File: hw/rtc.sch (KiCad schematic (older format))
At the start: 5 parts, among them U5 PCF8563T, Y1 Crystal_Small

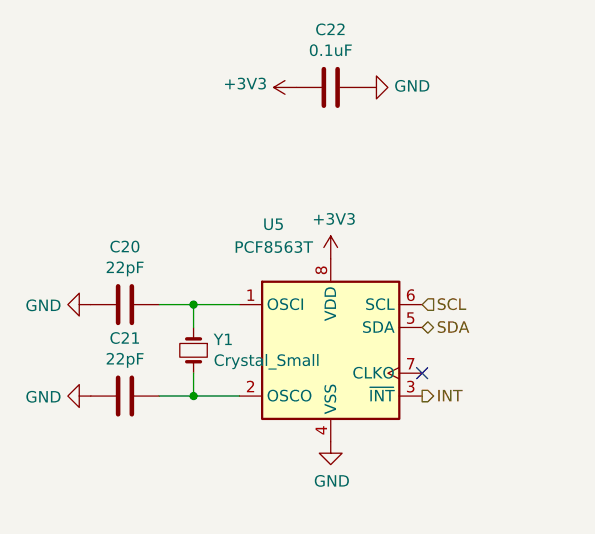
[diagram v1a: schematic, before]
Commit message: epd-clock: hw add wakeup pin pull up register
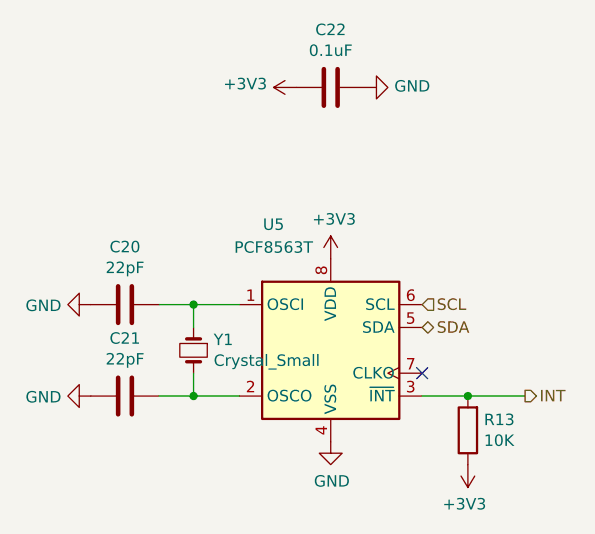
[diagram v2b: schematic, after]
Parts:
- added R13: 10K, Resistor_SMD:R_0603_1608Metric, symbol Device:R
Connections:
- net +3V3: now also R13.1
- net INT: now also R13.2
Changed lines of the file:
@@
 Text HLabel 6100 3800 2    50   BiDi ~ 0
 SDA
-Text HLabel 6100 4100 2    50   Output ~ 0
+Text HLabel 6550 4100 2    50   Output ~ 0
 INT
 NoConn ~ 6100 4000
+$Comp
+L Device:R R13
+U 1 1 6118B5C6
+P 6300 4250
+F 0 "R13" H 6230 4204 50  0000 R CNN
+F 1 "10K" H 6230 4295 50  0000 R CNN
+F 2 "Resistor_SMD:R_0603_1608Metric" V 6230 4250 50  0001 C CNN
+F 3 "~" H 6300 4250 50  0001 C CNN
+	1    6300 4250
+	-1   0    0    1
+$EndComp
+Wire Wire Line
+	6100 4100 6300 4100
+Connection ~ 6300 4100
+Wire Wire Line
+	6300 4100 6550 4100
+$Comp
+L power:+3V3 #PWR056
+U 1 1 6118BF3A
+P 6300 4400
+F 0 "#PWR056" H 6300 4250 50  0001 C CNN
+F 1 "+3V3" H 6315 4573 50  0000 C CNN
+F 2 "" H 6300 4400 50  0001 C CNN
+F 3 "" H 6300 4400 50  0001 C CNN
+	1    6300 4400
+	-1   0    0    1
+$EndComp
 $EndSCHEMATC

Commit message: epd-clock: hw: v0.2
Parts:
- renumbered C20 to C19, C21 to C20, C22 to C21, R13 to R18, U5 to U4
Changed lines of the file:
@@
 $EndDescr
 $Comp
-L Timer_RTC:PCF8563T U5
+L Timer_RTC:PCF8563T U4
 U 1 1 6123A351
 P 5700 3900
-F 0 "U5" H 5450 4450 50  0000 C CNN
+F 0 "U4" H 5450 4450 50  0000 C CNN
 F 1 "PCF8563T" H 5450 4350 50  0000 C CNN
 F 2 "Package_SO:SOIC-8_3.9x4.9mm_P1.27mm" H 5700 3900 50  0001 C CNN
@@
 $EndComp
 $Comp
-L Device:C C22
+L Device:C C21
 U 1 1 61243BFA
 P 5700 2750
-F 0 "C22" V 5448 2750 50  0000 C CNN
+F 0 "C21" V 5448 2750 50  0000 C CNN
 F 1 "0.1uF" V 5539 2750 50  0000 C CNN
 F 2 "Capacitor_SMD:C_0603_1608Metric" H 5738 2600 50  0001 C CNN
@@
 $EndComp
 $Comp
-L power:GND #PWR055
+L power:GND #PWR053
 U 1 1 61244BCB
 P 5850 2750
-F 0 "#PWR055" H 5850 2500 50  0001 C CNN
+F 0 "#PWR053" H 5850 2500 50  0001 C CNN
 F 1 "GND" V 5855 2622 50  0000 R CNN
 F 2 "" H 5850 2750 50  0001 C CNN
@@
 $EndComp
 $Comp
-L power:+3V3 #PWR052
+L power:+3V3 #PWR050
 U 1 1 6124514E
 P 5550 2750
-F 0 "#PWR052" H 5550 2600 50  0001 C CNN
+F 0 "#PWR050" H 5550 2600 50  0001 C CNN
 F 1 "+3V3" V 5565 2878 50  0000 L CNN
 F 2 "" H 5550 2750 50  0001 C CNN
@@
 $EndComp
 $Comp
-L power:+3V3 #PWR053
+L power:+3V3 #PWR051
 U 1 1 6124583B
 P 5700 3500
-F 0 "#PWR053" H 5700 3350 50  0001 C CNN
+F 0 "#PWR051" H 5700 3350 50  0001 C CNN
 F 1 "+3V3" H 5715 3673 50  0000 C CNN
 F 2 "" H 5700 3500 50  0001 C CNN
@@
 $EndComp
 $Comp
-L power:GND #PWR054
+L power:GND #PWR052
 U 1 1 61245C79
 P 5700 4300
-F 0 "#PWR054" H 5700 4050 50  0001 C CNN
+F 0 "#PWR052" H 5700 4050 50  0001 C CNN
 F 1 "GND" H 5705 4127 50  0000 C CNN
 F 2 "" H 5700 4300 50  0001 C CNN
@@
 $EndComp
 $Comp
-L Device:C C20
+L Device:C C19
 U 1 1 612485A7
 P 4800 3700
-F 0 "C20" V 4548 3700 50  0000 C CNN
+F 0 "C19" V 4548 3700 50  0000 C CNN
 F 1 "22pF" V 4639 3700 50  0000 C CNN
 F 2 "Capacitor_SMD:C_0603_1608Metric" H 4838 3550 50  0001 C CNN
@@
 $EndComp
 $Comp
-L Device:C C21
+L Device:C C20
 U 1 1 61248D49
 P 4800 4100
-F 0 "C21" V 4548 4100 50  0000 C CNN
+F 0 "C20" V 4548 4100 50  0000 C CNN
 F 1 "22pF" V 4639 4100 50  0000 C CNN
 F 2 "Capacitor_SMD:C_0603_1608Metric" H 4838 3950 50  0001 C CNN
@@
 	5100 3700 5300 3700
 $Comp
-L power:GND #PWR050
+L power:GND #PWR048
 U 1 1 61249AC1
 P 4650 3700
-F 0 "#PWR050" H 4650 3450 50  0001 C CNN
+F 0 "#PWR048" H 4650 3450 50  0001 C CNN
 F 1 "GND" V 4655 3572 50  0000 R CNN
 F 2 "" H 4650 3700 50  0001 C CNN
@@
 $EndComp
 $Comp
-L power:GND #PWR051
+L power:GND #PWR049
 U 1 1 61249FBE
 P 4650 4100
-F 0 "#PWR051" H 4650 3850 50  0001 C CNN
+F 0 "#PWR049" H 4650 3850 50  0001 C CNN
 F 1 "GND" V 4655 3972 50  0000 R CNN
 F 2 "" H 4650 4100 50  0001 C CNN
@@
 NoConn ~ 6100 4000
 $Comp
-L Device:R R13
+L Device:R R18
 U 1 1 6118B5C6
 P 6300 4250
-F 0 "R13" H 6230 4204 50  0000 R CNN
+F 0 "R18" H 6230 4204 50  0000 R CNN
 F 1 "10K" H 6230 4295 50  0000 R CNN
 F 2 "Resistor_SMD:R_0603_1608Metric" V 6230 4250 50  0001 C CNN
@@
 	6300 4100 6550 4100
 $Comp
-L power:+3V3 #PWR056
+L power:+3V3 #PWR054
 U 1 1 6118BF3A
 P 6300 4400
-F 0 "#PWR056" H 6300 4250 50  0001 C CNN
+F 0 "#PWR054" H 6300 4250 50  0001 C CNN
 F 1 "+3V3" H 6315 4573 50  0000 C CNN
 F 2 "" H 6300 4400 50  0001 C CNN

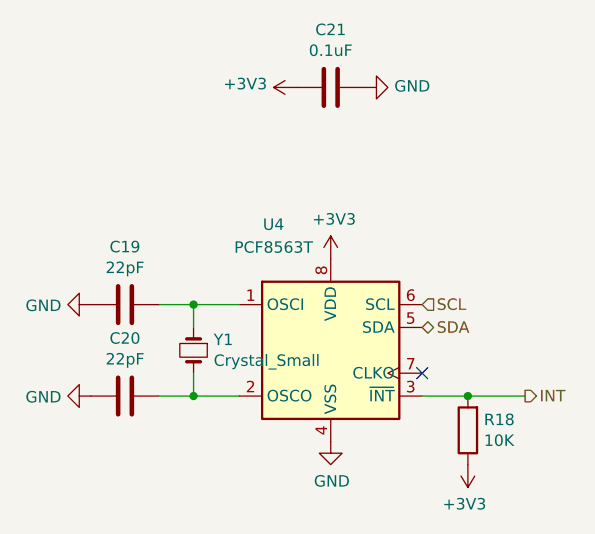
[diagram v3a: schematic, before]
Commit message: hw: 合并电源网络
取消墨水屏电源控制mos与独立电源域，墨水屏使用深度休眠模式，共用主
电源域。
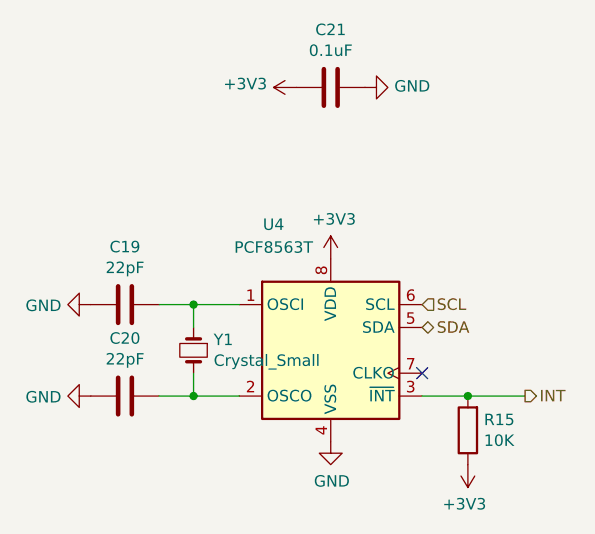
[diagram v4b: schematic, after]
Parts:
- renumbered R18 to R15
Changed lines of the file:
@@
 $EndComp
 $Comp
-L power:GND #PWR053
+L power:GND #PWR051
 U 1 1 61244BCB
 P 5850 2750
-F 0 "#PWR053" H 5850 2500 50  0001 C CNN
+F 0 "#PWR051" H 5850 2500 50  0001 C CNN
 F 1 "GND" V 5855 2622 50  0000 R CNN
 F 2 "" H 5850 2750 50  0001 C CNN
@@
 $EndComp
 $Comp
-L power:+3V3 #PWR050
+L power:+3V3 #PWR048
 U 1 1 6124514E
 P 5550 2750
-F 0 "#PWR050" H 5550 2600 50  0001 C CNN
+F 0 "#PWR048" H 5550 2600 50  0001 C CNN
 F 1 "+3V3" V 5565 2878 50  0000 L CNN
 F 2 "" H 5550 2750 50  0001 C CNN
@@
 $EndComp
 $Comp
-L power:+3V3 #PWR051
+L power:+3V3 #PWR049
 U 1 1 6124583B
 P 5700 3500
-F 0 "#PWR051" H 5700 3350 50  0001 C CNN
+F 0 "#PWR049" H 5700 3350 50  0001 C CNN
 F 1 "+3V3" H 5715 3673 50  0000 C CNN
 F 2 "" H 5700 3500 50  0001 C CNN
@@
 $EndComp
 $Comp
-L power:GND #PWR052
+L power:GND #PWR050
 U 1 1 61245C79
 P 5700 4300
-F 0 "#PWR052" H 5700 4050 50  0001 C CNN
+F 0 "#PWR050" H 5700 4050 50  0001 C CNN
 F 1 "GND" H 5705 4127 50  0000 C CNN
 F 2 "" H 5700 4300 50  0001 C CNN
@@
 	5100 3700 5300 3700
 $Comp
-L power:GND #PWR048
+L power:GND #PWR046
 U 1 1 61249AC1
 P 4650 3700
-F 0 "#PWR048" H 4650 3450 50  0001 C CNN
+F 0 "#PWR046" H 4650 3450 50  0001 C CNN
 F 1 "GND" V 4655 3572 50  0000 R CNN
 F 2 "" H 4650 3700 50  0001 C CNN
@@
 $EndComp
 $Comp
-L power:GND #PWR049
+L power:GND #PWR047
 U 1 1 61249FBE
 P 4650 4100
-F 0 "#PWR049" H 4650 3850 50  0001 C CNN
+F 0 "#PWR047" H 4650 3850 50  0001 C CNN
 F 1 "GND" V 4655 3972 50  0000 R CNN
 F 2 "" H 4650 4100 50  0001 C CNN
@@
 NoConn ~ 6100 4000
 $Comp
-L Device:R R18
+L Device:R R15
 U 1 1 6118B5C6
 P 6300 4250
-F 0 "R18" H 6230 4204 50  0000 R CNN
+F 0 "R15" H 6230 4204 50  0000 R CNN
 F 1 "10K" H 6230 4295 50  0000 R CNN
 F 2 "Resistor_SMD:R_0603_1608Metric" V 6230 4250 50  0001 C CNN
@@
 	6300 4100 6550 4100
 $Comp
-L power:+3V3 #PWR054
+L power:+3V3 #PWR052
 U 1 1 6118BF3A
 P 6300 4400
-F 0 "#PWR054" H 6300 4250 50  0001 C CNN
+F 0 "#PWR052" H 6300 4250 50  0001 C CNN
 F 1 "+3V3" H 6315 4573 50  0000 C CNN
 F 2 "" H 6300 4400 50  0001 C CNN
